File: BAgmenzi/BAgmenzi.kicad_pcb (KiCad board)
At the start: 6 copper layers, 64.8 x 44.8 mm, 155 parts, among them IC1 TPL0501-100RSER, J1 Conn_01x07, J2 DF52-2S-0.8H(21), J3 USB3076-30-A, J5 3220-10-0100-00, Q1 NX7002BKMBYL, U1 MSP430FR5043IRGCT, U10 PESD1USB30, U11 MAX77654BENV+T, U13 TPS7A2033DBVDQN, U2 AD8338ACPZ-R7, U3 OPA836IDBVT, U4 OPA836IDBVT, U5 polyCMUT, U6 DNP, U7 LT3463AEDD#PBF, U8 TPS22916CYFPR, U9 MAXM86161EFD_T, X1 FY0800018, X2 ABS07-32.768KHZ-9-T, Y1 AWSCR-8.00CV-T

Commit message: edge cuts
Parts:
- added REF**: MouseBite-Part_2.0x2.0mm_inset_D0.5mm_P0.85mm_5h, Panelization:MouseBite-Part_2.0x2.0mm_inset_D0.5mm_P0.85mm_5h, F.Cu at (118.3, 103.5)
- added REF**: MouseBite-Part_2.0x2.0mm_inset_D0.5mm_P0.85mm_4h_Trace, Panelization:MouseBite-Part_2.0x2.0mm_inset_D0.5mm_P0.85mm_4h_Trace, F.Cu at (130.4, 124.8)
- added REF**: MouseBite-Part_2.0x2.0mm_inset_D0.5mm_P0.85mm_4h_Trace, Panelization:MouseBite-Part_2.0x2.0mm_inset_D0.5mm_P0.85mm_4h_Trace, F.Cu at (118.3, 99.5)
- added REF**: MouseBite-Part_2.0x2.0mm_inset_D0.5mm_P0.85mm_5h, Panelization:MouseBite-Part_2.0x2.0mm_inset_D0.5mm_P0.85mm_5h, F.Cu at (136.6, 124.8)
- added REF**: MouseBite-Part_2.0x4.5mm_inset_D0.5mm_P0.85mm_5h_Trace, Panelization:MouseBite-Part_2.0x4.5mm_inset_D0.5mm_P0.85mm_5h_Trace, F.Cu at (124.3, 124.8)
- moved R45 1.20 mm to (115.6, 105.5), turned to -90 degrees
- moved J5 1.13 mm to (110.8, 102.6)
- moved R46 1.01 mm to (115.7, 103.3), turned to 90 degrees
- moved JP4 0.18 mm to (157.4, 97.5)
- moved C21 0.18 mm to (134.6, 104.8)
- moved R41 0.13 mm to (159.0, 95.5)
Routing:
- net GND: track 151.9 -> 154.2 mm, vias 108 -> 110
- net Net-(X1-IN/OUT): track 5.04 -> 3.03 mm
- net SWCLK: track 5.89 -> 7.28 mm
- net /RX/VGA_REF: track 25.0 -> 23.6 mm
- net nRST: track 46.4 -> 47.6 mm
- net SWDIO: track 20.5 -> 21.5 mm
- net Net-(J5-Pad2): track 3.30 -> 3.85 mm
- net Net-(J5-Pad4): track 2.44 -> 3.00 mm
- net DVDD_3.3: track 74.1 -> 73.6 mm
- added copper zone on In2.Cu, net GND
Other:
- board size 64.8 x 44.8 mm -> 66.3 x 44.2 mm

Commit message: edgecuts/DCR check
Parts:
- moved R46 0.38 mm to (115.3, 103.2)
- moved R45 0.35 mm to (115.3, 105.5)
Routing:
- net Net-(D2-K): track 3.44 -> 5.99 mm
- net DVDD_3.3: track 73.6 -> 75.8 mm, vias 20 -> 21
- net GND: track 154.2 -> 155.2 mm, vias 110 -> 147
- net /TX/PULSER_OUT: track 1.26 -> 2.22 mm
- net /RX/BUF_OUT: track 3.36 -> 3.96 mm
- net /RX/VGA_OUT: track 2.95 -> 2.38 mm
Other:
- outline, holes or cut-outs redrawn

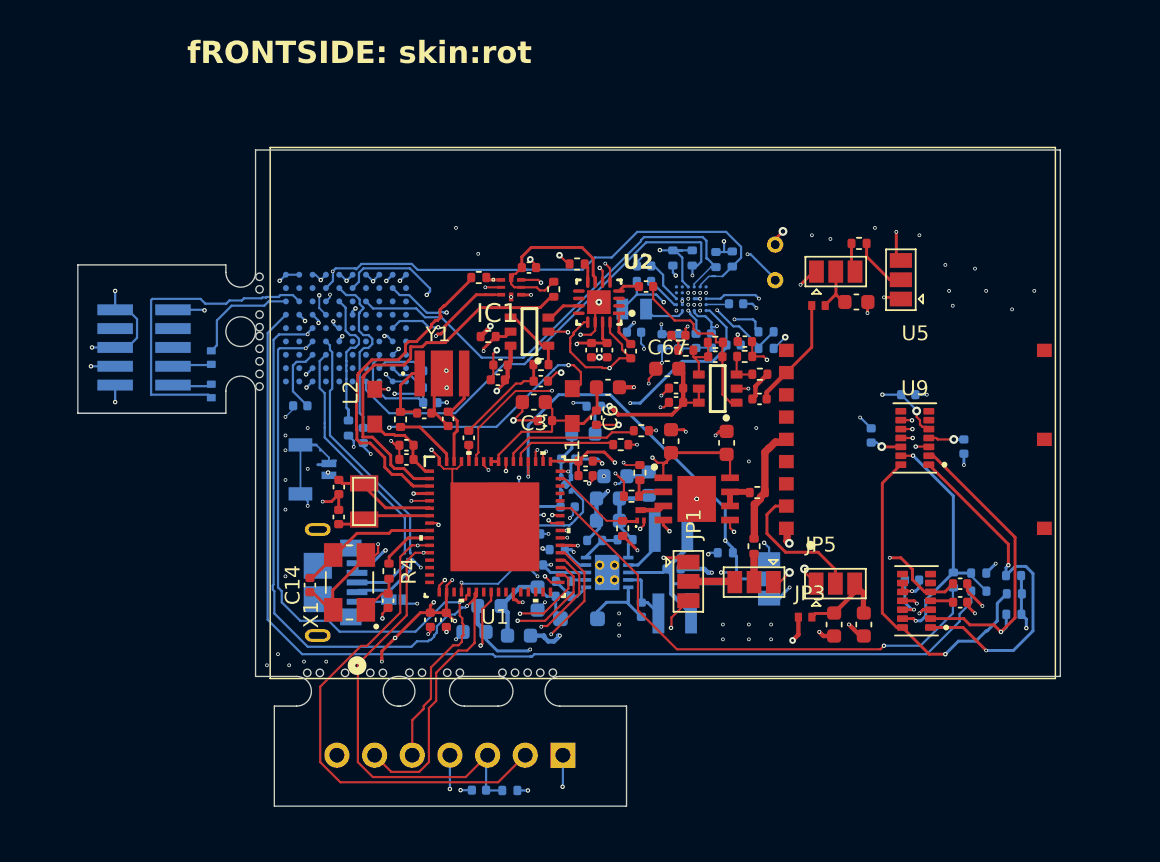
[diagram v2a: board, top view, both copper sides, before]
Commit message: corrected LCSC numbers, other changes, Testpoints
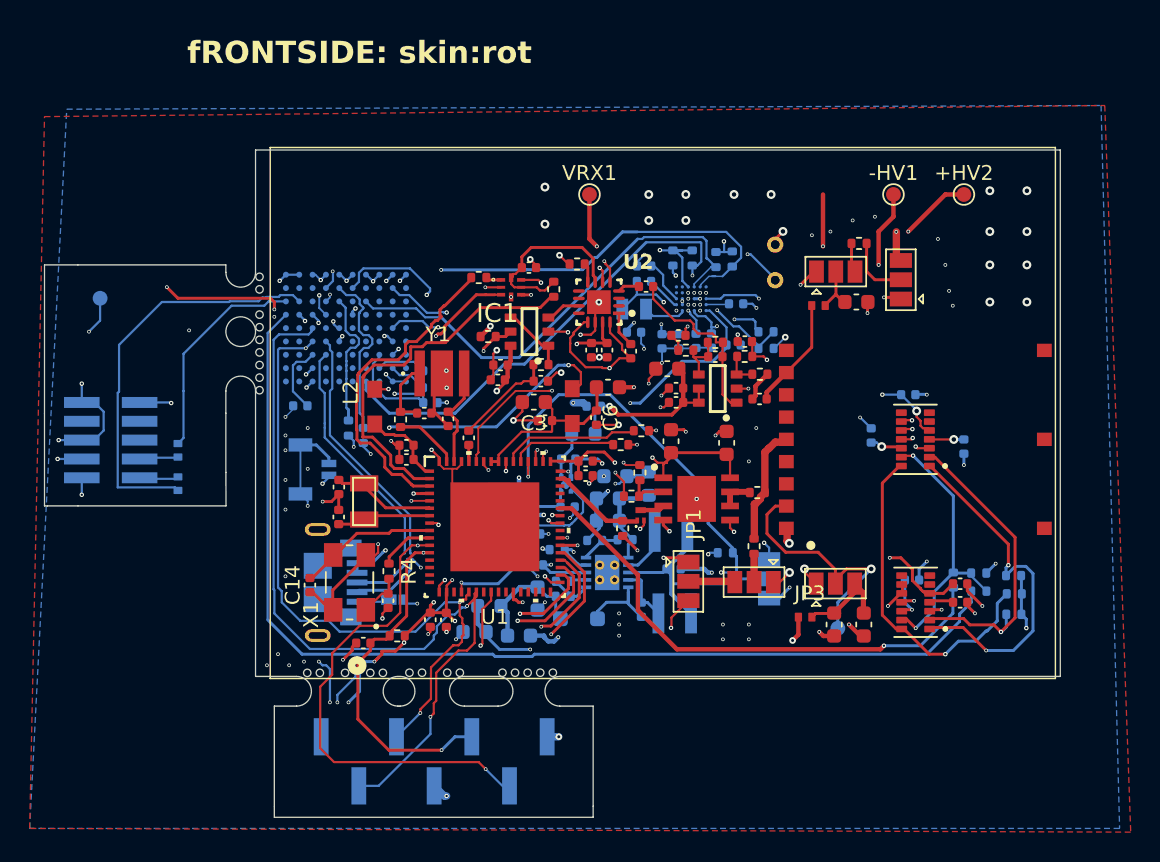
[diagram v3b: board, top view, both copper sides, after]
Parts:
- added +HV2: TestPoint, TestPoint:TestPoint_Pad_D1.0mm, F.Cu at (166.1, 92.2)
- added -HV1: TestPoint, TestPoint:TestPoint_Pad_D1.0mm, F.Cu at (161.3, 92.2)
- added DVDD1: TestPoint, TestPoint:TestPoint_Pad_D1.0mm, B.Cu at (107.8, 99.2)
- added TP8: BOT_EL, TestPoint:TestPoint_Pad_D1.0mm, B.Cu at (157.6, 121.5)
- added VRX1: TestPoint, TestPoint:TestPoint_Pad_D1.0mm, F.Cu at (140.8, 92.2)
- C2, R1: moved to F.Cu
- J1: footprint Connector_PinHeader_2.54mm:PinHeader_1x07_P2.54mm_Vertical -> Connector_PinHeader_2.54mm:PinHeader_1x07_P2.54mm_Vertical_SMD_Pin1Right
- L5, L6: value LQG15HS3N9B02D -> LQH3NPZ100MMEL
- U13: value TPS7A2033DBVDQN -> TPS7A2033PDQNR
- moved R1 12.9 mm to (127.8, 122.0)
- moved C2 12.6 mm to (125.5, 122.5)
- moved J1 8.69 mm to (130.3, 130.5)
- moved J5 6.64 mm to (108.5, 108.8)
- moved R45 6.64 mm to (113.0, 111.8)
- moved R46 6.64 mm to (113.0, 109.5)
- moved REF** 0.25 mm to (118.3, 103.8)
- moved U6 0.11 mm to (162.8, 119.8)
- moved U9 0.10 mm to (162.8, 108.8)
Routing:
- net GND: track 155.2 -> 169.6 mm, vias 147 -> 157
- net DVDD_3.3: track 75.8 -> 86.8 mm, vias 21 -> 24
- net Net-(JP5-C): track 9.40 -> 17.3 mm, vias 0 -> 1
- net nRST: track 47.6 -> 55.4 mm, vias 2 -> 3
- net SWCLK: track 7.39 -> 14.6 mm
- net JTAG.RESET_N: track 40.2 -> 33.5 mm, vias 2 -> 3
- net SWDIO: track 21.1 -> 27.5 mm
- net +HV: track 14.1 -> 19.3 mm, vias 4 -> 5
- net -HV: track 12.0 -> 16.1 mm, vias 4 -> 5
- net V_LED: track 15.3 -> 19.1 mm, vias 5 -> 6
- net V_RX: track 22.5 -> 26.2 mm, vias 5 -> 6
- net PMIC_I2C.SCL: track 27.4 -> 25.3 mm
- net JTAG.TEST: track 42.5 -> 41.1 mm, vias 2 -> 3
- net BSL.UART_TX: track 46.5 -> 45.7 mm, vias 2 -> 3
- net V_BAT: track 8.11 -> 8.83 mm
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- added copper zone on B.Cu, net GND
- added copper zone on F.Cu, net GND
- removed copper zone on In1.Cu, net (none)
- removed copper zone on In4.Cu, net (none)
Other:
- board size 66.3 x 44.2 mm -> 68.5 x 45 mm
- board text added: "VBAT"
- board text added: "VSYS"
